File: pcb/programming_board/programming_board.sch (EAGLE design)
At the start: 34 parts

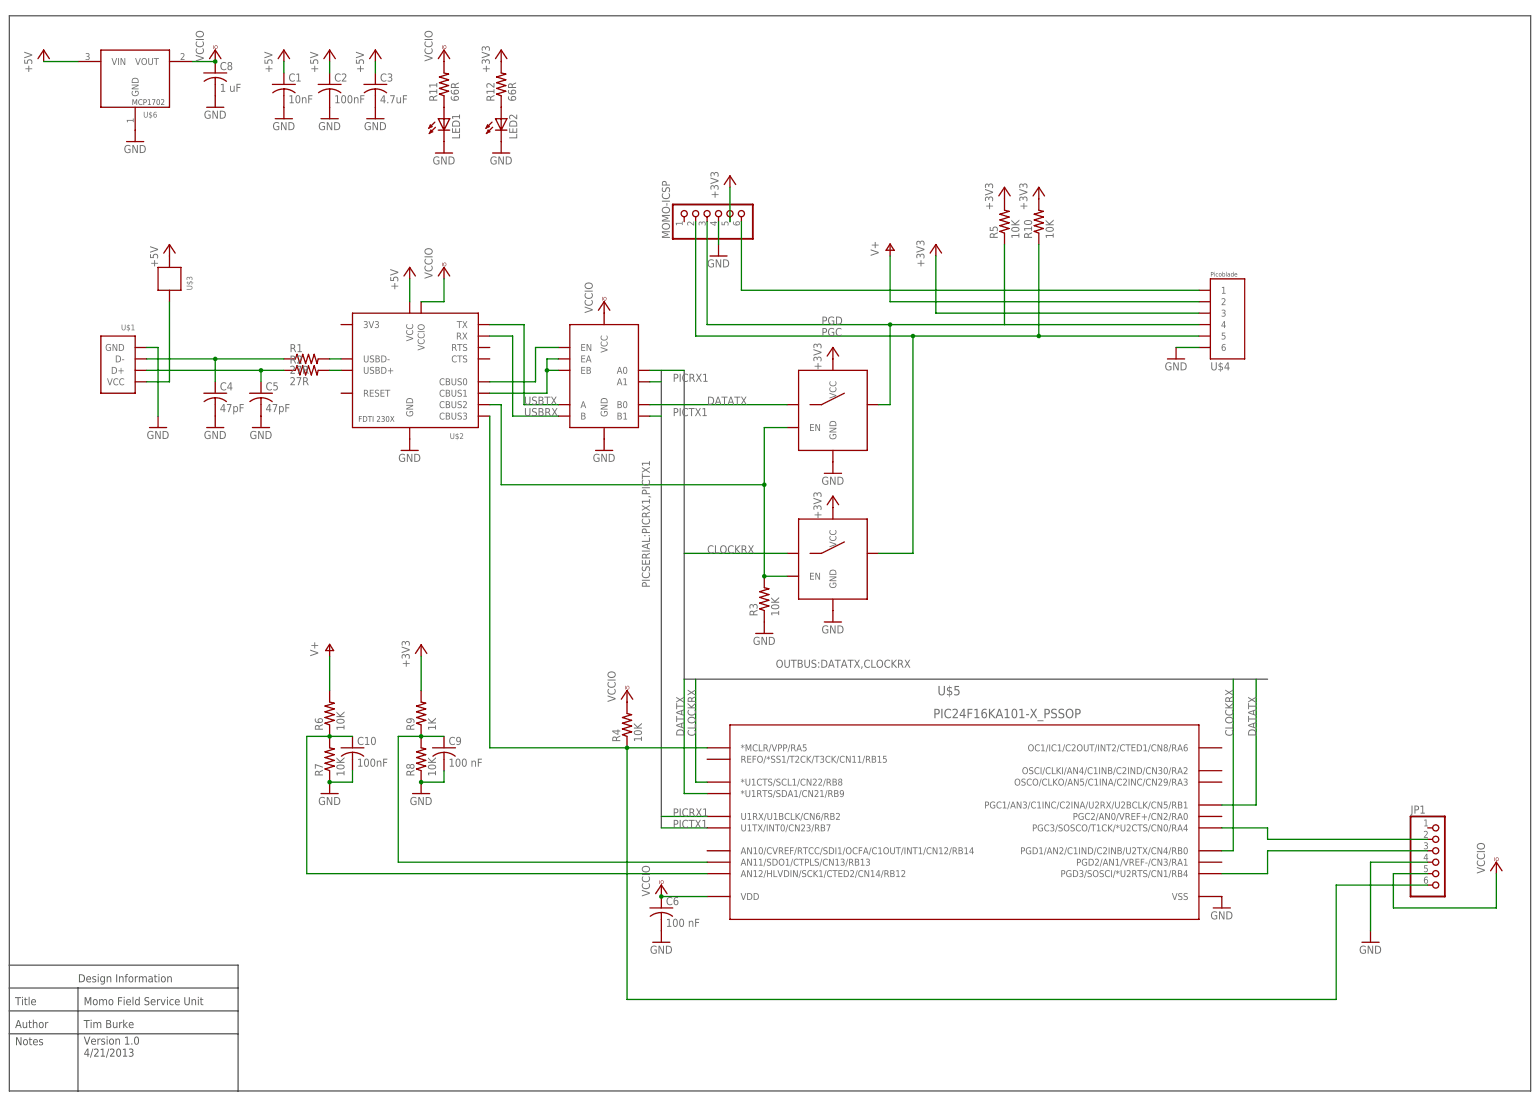
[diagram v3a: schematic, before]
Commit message: Updated MoMo FSU to version 2.  Following major changes: 1. Removed unneeded header for momo programming. 2. Removed mux and analog switches allowing serial passthrough, all communication with momo will be over mib. 3. standardized momo connector 4. relaid out board
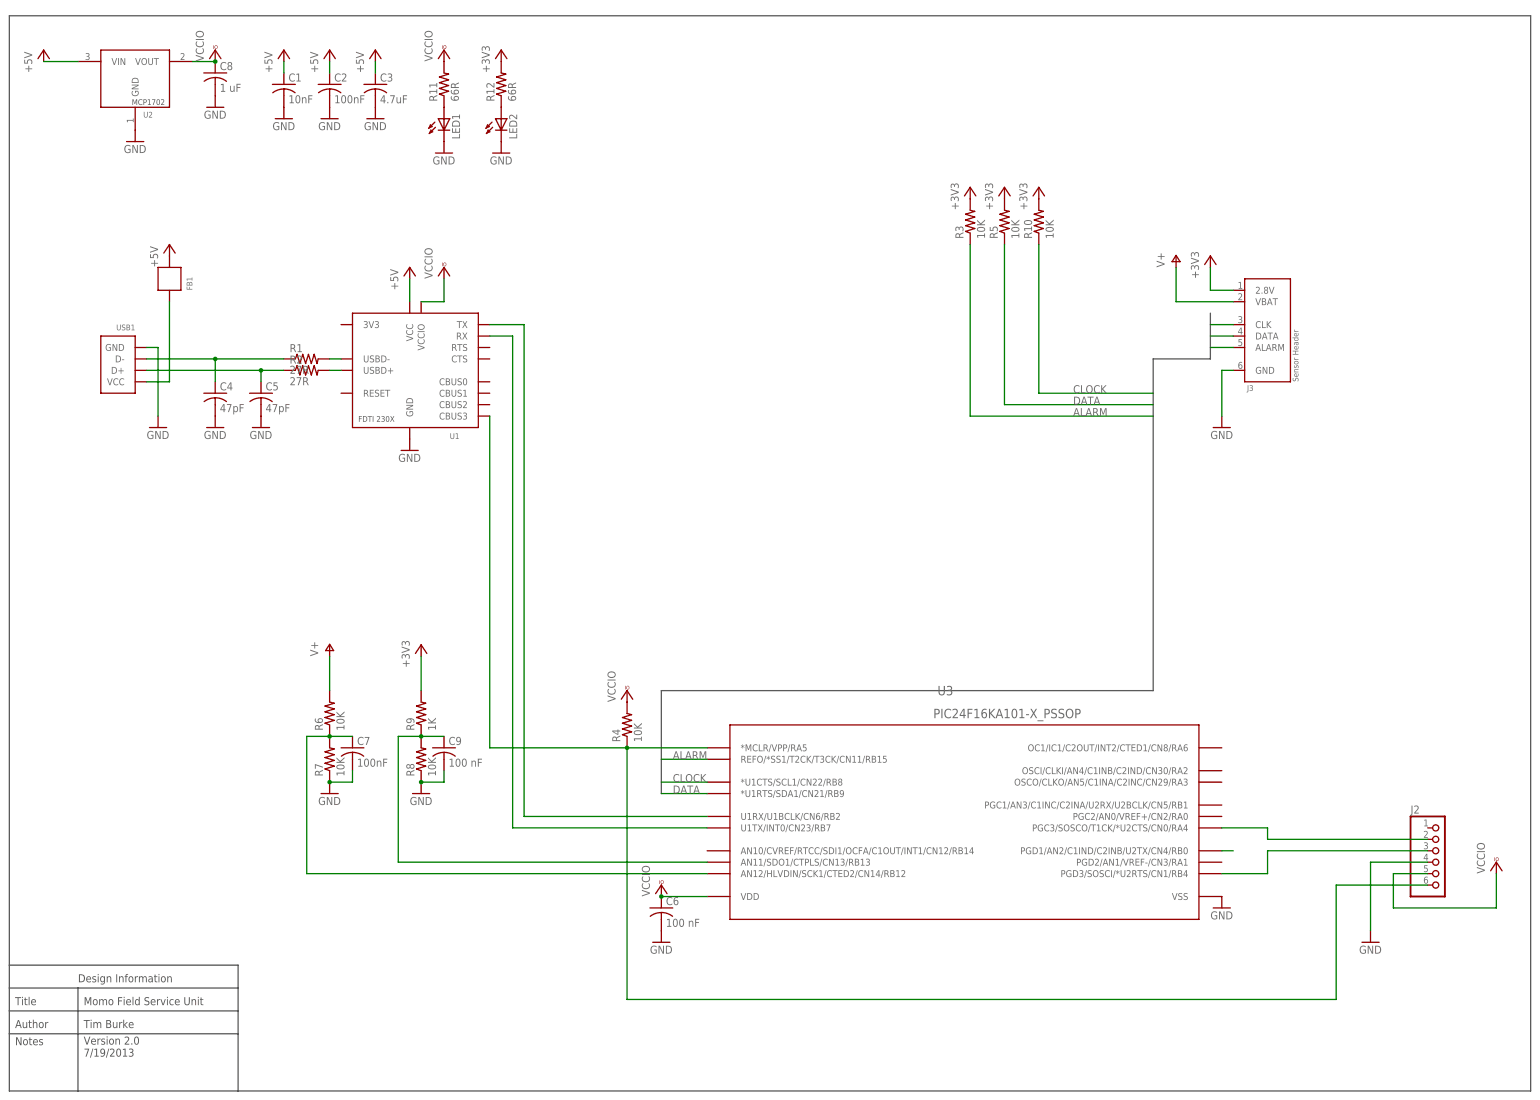
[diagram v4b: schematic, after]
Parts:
- removed MOMO-ICSP: (no value), pinhead:PINHD-1X6/90
- removed U$4: 2X3-MOLEX-90130, components:2X3-MOLEX-90130
- removed U$7: DG636, components:DG636
- removed U$8, U$9: TS5A1066-SPST, components:TS5A1066-SPST
- added J3: MOMO-SENSOR-HEADER, components:MOMO-SENSOR-HEADER
- renumbered C10 to C7, JP1 to J2, U$1 to USB1, U$2 to U1, U$3 to FB1, U$5 to U3, U$6 to U2
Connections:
- removed net DATATX: U$7.B0, U$8.COM, U3.*U1RTS/SDA1/CN21/RB9, U3.PGC1/AN3/C1INC/C2INA/U2RX/U2BCLK/CN5/RB1
- removed net N$10: U$7.EN, U1.CBUS0
- removed net N$11: U$7.EA, U$7.EB, U1.CBUS1
- removed net N$6: MOMO-ICSP.6, U$4.1
- removed net N$7: R3.2, U$8.EN, U$9.EN, U1.CBUS2
- removed net PGC: MOMO-ICSP.2, R10.1, U$4.5, U$9.NO
- removed net PGD: MOMO-ICSP.3, R5.1, U$4.4, U$8.NO
- removed net USBRX: U$7.B, U1.RX
- removed net USBTX: U$7.A, U1.TX
- new net ALARM: J3.ALARM, R3.1, U3.REFO/*SS1/T2CK/T3CK/CN11/RB15
- new net CLOCK: J3.CLK, R10.1, U3.*U1CTS/SCL1/CN22/RB8
- new net DATA: J3.DATA, R5.1, U3.*U1RTS/SDA1/CN21/RB9
- net +3V3: now also J3.2.8V, R3.2; no longer MOMO-ICSP.5, U$4.3, U$8.VCC, U$9.VCC
- net CLOCKRX: no longer U$7.A0, U$9.COM, U3.*U1CTS/SCL1/CN22/RB8
- net GND: now also J3.GND; no longer MOMO-ICSP.4, R3.1, U$4.6, U$7.GND, U$8.GND, U$9.GND
- net PICRX1: now also U1.TX; no longer U$7.A1
- net PICTX1: now also U1.RX; no longer U$7.B1
- net V+: now also J3.VBAT; no longer U$4.2
- net VCCIO: no longer U$7.VCC
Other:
- note added: "Version 2.0 7/19/2013"
- note removed: "Version 1.0 4/21/2013"
- moved on the sheet: R3

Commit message: Update MoMo FSU with modular connector
- relay out to fix Polycase USB-31 case.
- board is finished and ready for fabrication
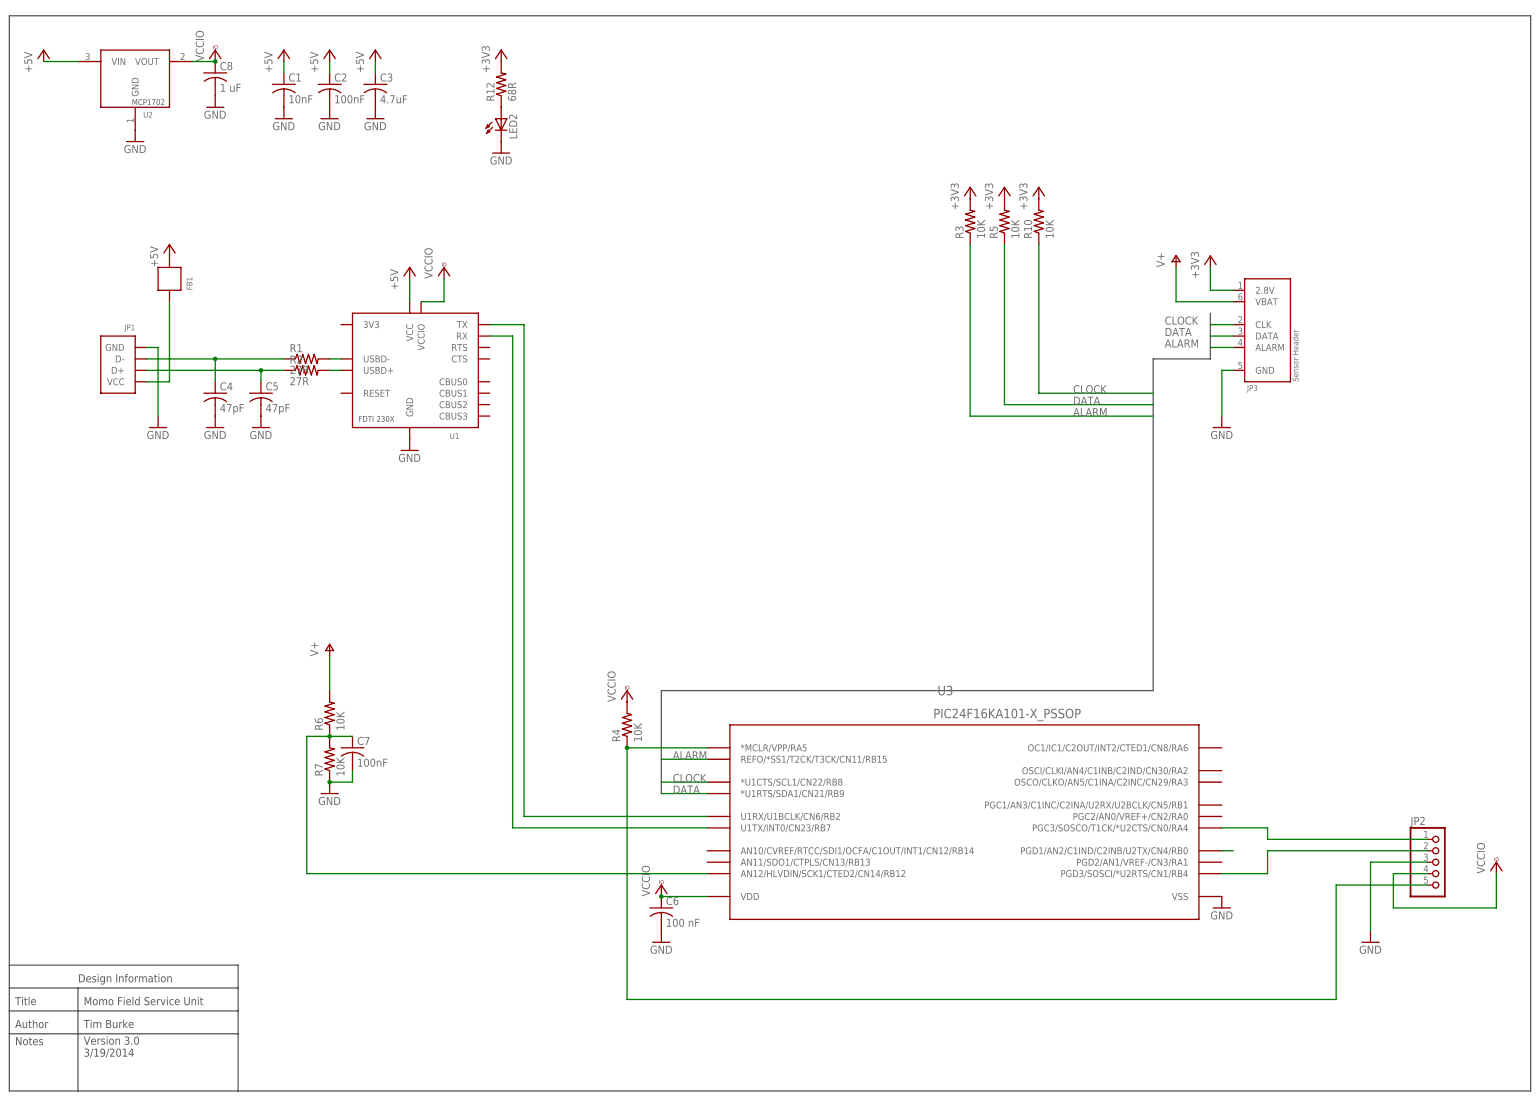
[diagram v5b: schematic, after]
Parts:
- removed C9: 100 nF, rcl:C-USC0402
- removed J2: (no value), pinhead:PINHD-1X6/90
- removed J3: MOMO-SENSOR-HEADER, components:MOMO-SENSOR-HEADER
- removed LED1: (no value), led:LED5MM
- removed R11: 66R, rcl:R-US_R0603
- removed R8: 10K, rcl:R-US_R0603
- removed R9: 1K, rcl:R-US_R0603
- removed USB1: USB-A, components:USB-A
- added JP1: MOLEX-USB-CONN, components:MOLEX-USB-CONN
- added JP2: (no value), pinhead:PINHD-1X5
- added JP3: MOMO-SENSOR-RJ11-VERT, components:MOMO-SENSOR-RJ11-VERT
- C1: DIGIKEY-PN (none) -> 1276-1499-1-ND
- C2, C6, C7: DIGIKEY-PN (none) -> 445-1265-1-ND
- C3: DIGIKEY-PN (none) -> 445-1605-1-ND
- C4, C5: DIGIKEY-PN (none) -> 1276-1699-1-ND
- C8: DIGIKEY-PN (none) -> 1276-1076-1-ND
- FB1: DESCRIPTION (none) -> Ferrite Bead; DIGIKEY-PN (none) -> 240-2390-1-ND; FOOTPRINT (none) -> SMD 0805
- LED2: device led:LED5MM -> led:LEDSML0603; DESCRIPTION (none) -> Green Chip LED; DIGIKEY-PN (none) -> 475-1409-1-ND; FOOTPRINT (none) -> SMD 0603
- R1, R2: DIGIKEY-PN (none) -> P27.0HCT-ND
- R10, R3, R4, R5, R6, R7: DIGIKEY-PN (none) -> P10.0KHCT-ND
- R12: value 66R -> 68R; DIGIKEY-PN (none) -> P68GCT-ND
- U1: DESCRIPTION (none) -> FTDI-230X USB-Serial Adapter IC; DIGIKEY-PN (none) -> 768-1135-1-ND; FOOTPRINT (none) -> SSOP16
- U3: DESCRIPTION (none) -> PIC 24F16KA101 16-bit Microprocessor; DIGIKEY-PN (none) -> PIC24F16KA101-I/SS-ND; FOOTPRINT (none) -> SSOP20
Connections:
- removed net N$12: LED1.A, R11.1
- removed net N$20: C9.1, R8.2, R9.1, U3.AN11/SDO1/CTPLS/CN13/RB13
- net +3V3: now also JP3.2.8V; no longer J3.2.8V, R9.2
- net ALARM: now also JP3.ALARM; no longer J3.ALARM
- net CLOCK: now also JP3.CLK; no longer J3.CLK
- net DATA: now also JP3.DATA; no longer J3.DATA
- net GND: now also JP1.GND, JP2.3, JP3.GND; no longer C9.2, J2.4, J3.GND, LED1.C, R8.1, USB1.GND
- net N$1: now also JP1.D-; no longer USB1.D-
- net N$2: now also JP1.VCC; no longer USB1.VCC
- net N$21: now also JP2.5; no longer J2.6, U1.CBUS3
- net N$3: now also JP1.D+; no longer USB1.D+
- net N$8: now also JP2.1; no longer J2.2
- net N$9: now also JP2.2; no longer J2.3
- net V+: now also JP3.VBAT; no longer J3.VBAT
- net VCCIO: now also JP2.4; no longer J2.5, R11.2
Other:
- note added: "Version 3.0 3/19/2014"
- note removed: "Version 2.0 7/19/2013"
